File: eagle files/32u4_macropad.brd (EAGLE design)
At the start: 77.2 x 102.2 mm, 91 parts, among them J1 TYPE-C-31-M-12, Q1 16MHz, SW2 SWITCH-SMD-EVP-BB2A9B00

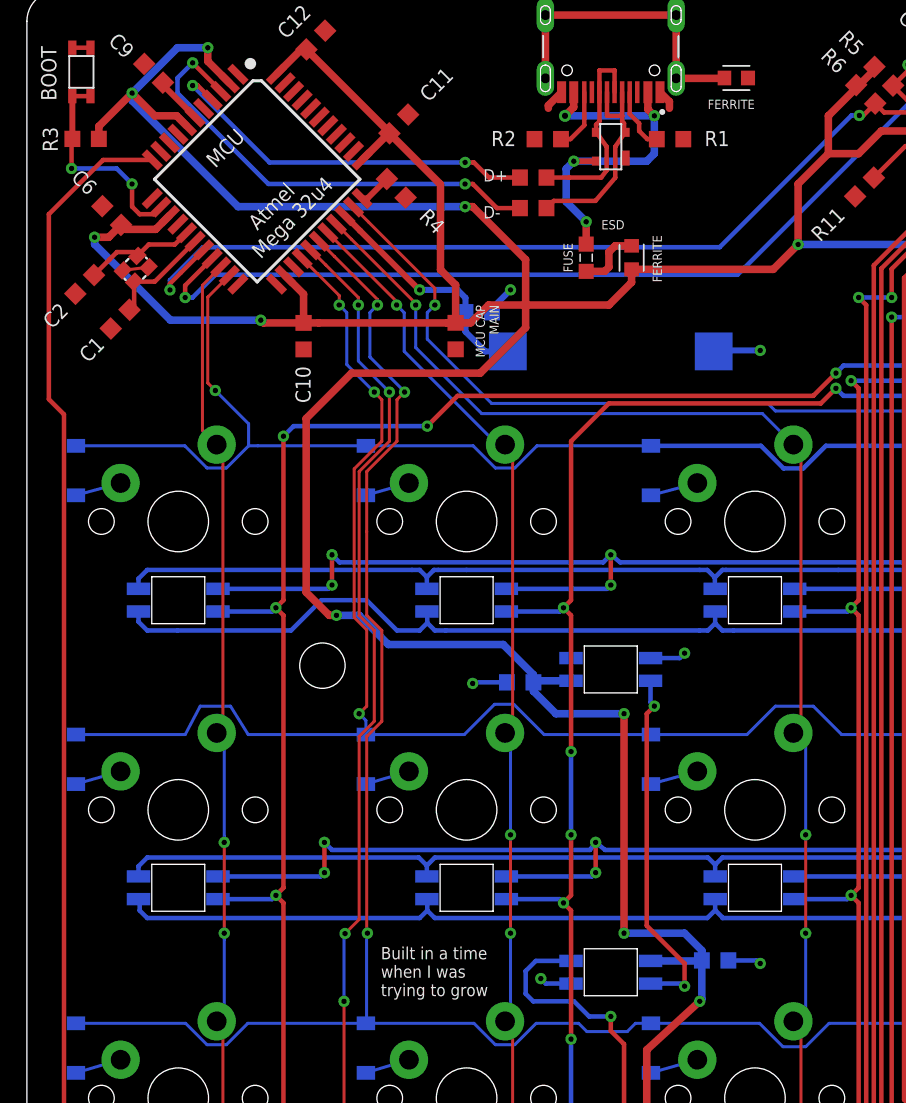
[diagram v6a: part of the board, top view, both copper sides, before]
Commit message: Component font size, routing adjustments
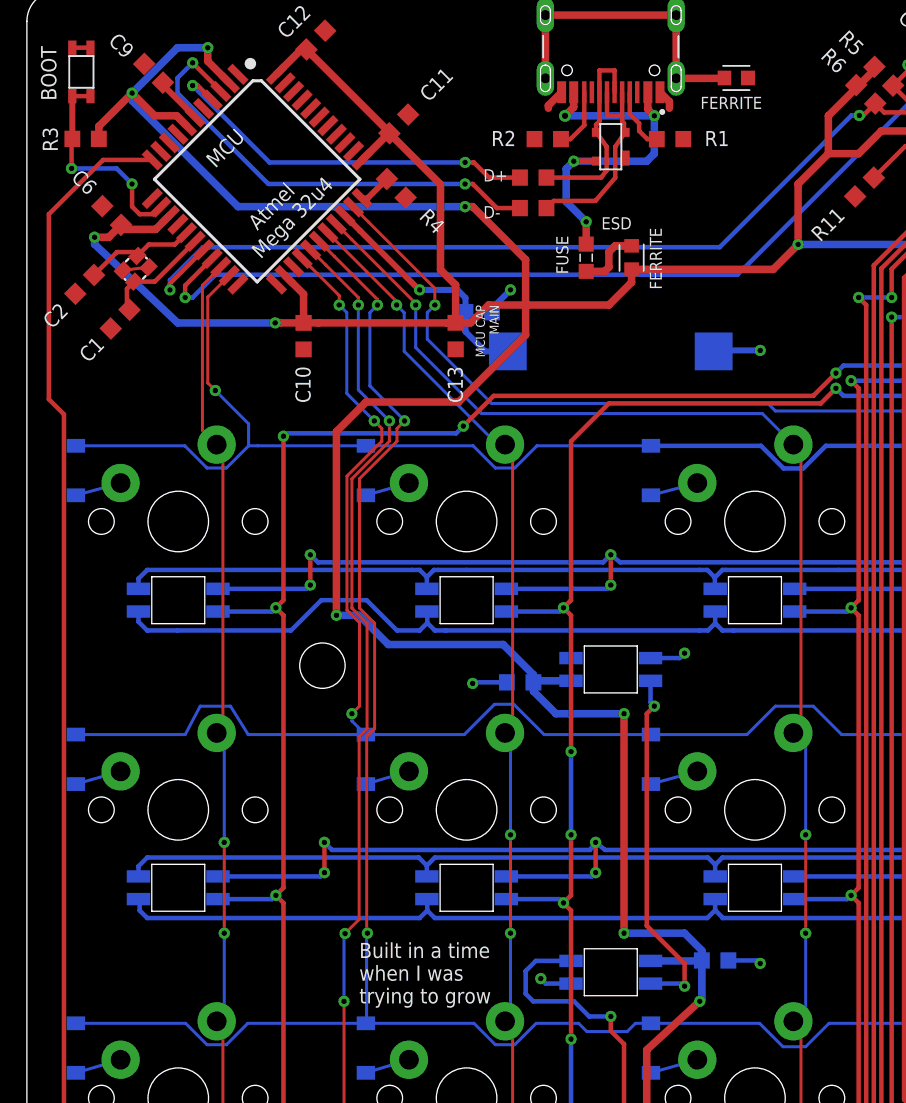
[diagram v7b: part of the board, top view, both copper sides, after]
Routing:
- net VCC: track 339.6 -> 336.2 mm

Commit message: Rev 1 start
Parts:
- moved C13 0.72 mm to (36.7, 88.5)
- moved R1 0.72 mm to (52.3, 101.5)
- moved R2 0.48 mm to (43.0, 101.5)
- moved C12 0.34 mm to (27.9, 108.2)
- moved R8 0.24 mm to (42.5, 97.1)
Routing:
- net VBUS: track 25.2 -> 20.6 mm
- net R0BLUE: track 89.0 -> 85.9 mm
- net VCC: track 336.2 -> 333.7 mm
- net C1RGB: track 129.8 -> 127.7 mm
- net C3SWTCH: track 117.3 -> 115.5 mm
- net C3RGB: track 101.1 -> 100.1 mm
- net N$24: track 28.8 -> 29.7 mm
- net R0SWTCH: track 73.8 -> 74.6 mm
- net N$17: track 14.2 -> 13.5 mm
- net R1SWTCH: track 97.9 -> 98.6 mm
- net R0RED: track 101.2 -> 100.6 mm
- net GND: track 52.4 -> 51.8 mm
- net C2SWTCH: track 96.6 -> 96.1 mm
